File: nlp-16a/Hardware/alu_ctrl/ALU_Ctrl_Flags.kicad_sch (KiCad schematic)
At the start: 18 parts, among them U1 CD74HC00, U10 CD74HC00, U11 CD74HC00, U12 CD74HC00, U13 CD74HC00, U14 CD74HC00, U15 CD74HC00, U16 CD74HC00, U17 CD74HC00, U18 CD74HC00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

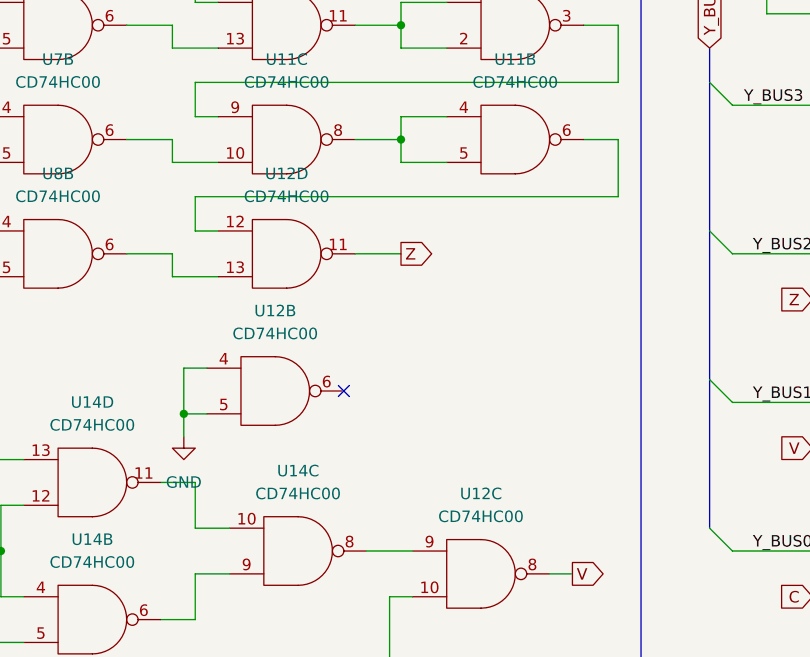
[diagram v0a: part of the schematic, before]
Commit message: ALU制御の回路修正
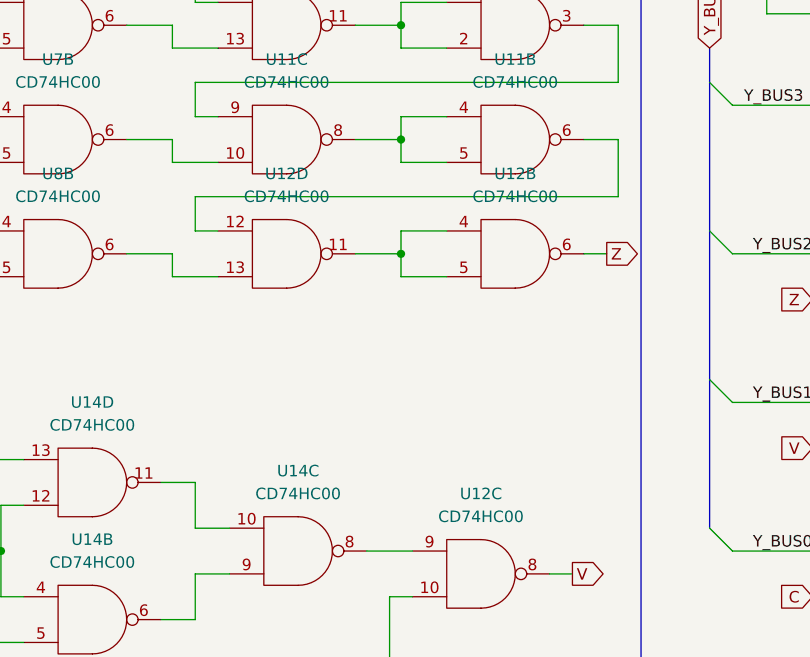
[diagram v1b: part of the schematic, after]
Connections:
- net GND: no longer U12.4, U12.5
- net Z: now also U12.6; no longer U12.11
- new net: U12.11, U12.4, U12.5
- no-connect marks 1 -> 0
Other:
- moved on the sheet: U12B
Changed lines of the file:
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@@
   (junction (at 64.77 22.86) (diameter 0) (color 0 0 0 0)
   )
+  (junction (at 163.83 116.84) (diameter 0) (color 0 0 0 0)
+  )
   (junction (at 163.83 91.44) (diameter 0) (color 0 0 0 0)
   )
@@
   (junction (at 36.83 53.34) (diameter 0) (color 0 0 0 0)
   )
-  (junction (at 139.7 134.62) (diameter 0) (color 0 0 0 0)
-  )
   (junction (at 212.09 90.17) (diameter 0) (color 0 0 0 0)
   )
@@
   (junction (at 163.83 66.04) (diameter 0) (color 0 0 0 0)
   )
-  (no_connect (at 157.48 132.08))
   (bus_entry (at 13.97 83.82) (size 2.54 2.54)
     (stroke (width 0) (type default) (color 0 0 0 0))
@@
     (stroke (width 0) (type default) (color 0 0 0 0))
   )
-  (wire (pts (xy 139.7 134.62) (xy 142.24 134.62))
+  (wire (pts (xy 163.83 119.38) (xy 168.91 119.38))
     (stroke (width 0) (type default) (color 0 0 0 0))
   )
@@
     (stroke (width 0) (type default) (color 0 0 0 0))
   )
-  (wire (pts (xy 142.24 129.54) (xy 139.7 129.54))
+  (wire (pts (xy 168.91 114.3) (xy 163.83 114.3))
     (stroke (width 0) (type default) (color 0 0 0 0))
   )
@@
     (stroke (width 0) (type default) (color 0 0 0 0))
   )
+  (wire (pts (xy 186.69 116.84) (xy 184.15 116.84))
+    (stroke (width 0) (type default) (color 0 0 0 0))
+  )
   (wire (pts (xy 35.56 137.16) (xy 38.1 137.16))
     (stroke (width 0) (type default) (color 0 0 0 0))
@@
     (stroke (width 0) (type default) (color 0 0 0 0))
   )
-  (wire (pts (xy 139.7 134.62) (xy 139.7 137.16))
-    (stroke (width 0) (type default) (color 0 0 0 0))
-  )
   (wire (pts (xy 64.77 68.58) (xy 64.77 63.5))
     (stroke (width 0) (type default) (color 0 0 0 0))
@@
     (stroke (width 0) (type default) (color 0 0 0 0))
   )
-  (wire (pts (xy 139.7 129.54) (xy 139.7 134.62))
+  (wire (pts (xy 163.83 114.3) (xy 163.83 116.84))
     (stroke (width 0) (type default) (color 0 0 0 0))
   )
@@
   )
   (wire (pts (xy 113.03 78.74) (xy 113.03 76.2))
+    (stroke (width 0) (type default) (color 0 0 0 0))
+  )
+  (wire (pts (xy 163.83 116.84) (xy 163.83 119.38))
     (stroke (width 0) (type default) (color 0 0 0 0))
   )
@@
     )
   )
-  (global_label "Z" (shape output) (at 163.83 116.84 0) (fields_autoplaced)
+  (global_label "Z" (shape output) (at 186.69 116.84 0) (fields_autoplaced)
     (effects (font (size 1.27 1.27)) (justify left))
-    (property "Intersheet References" "${INTERSHEET_REFS}" (id 0) (at 167.4526 116.7606 0)
+    (property "Intersheet References" "${INTERSHEET_REFS}" (id 0) (at 190.3126 116.7606 0)
       (effects (font (size 1.27 1.27)) (justify left) hide)
     )
@@
     (pin "13")
   )
-  (symbol (lib_id "CD74HCxx:CD74HC00") (at 149.86 132.08 0) (unit 2)
+  (symbol (lib_id "CD74HCxx:CD74HC00") (at 176.53 116.84 0) (unit 2)
     (in_bom yes) (on_board yes)
-    (property "Reference" "U12" (id 0) (at 149.86 123.19 0))
-    (property "Value" "CD74HC00" (id 1) (at 149.86 125.73 0))
-    (property "Footprint" "Package_DIP:DIP-14_W7.62mm" (id 2) (at 144.78 132.08 0)
-      (effects (font (size 1.27 1.27)) hide)
-    )
-    (property "Datasheet" "" (id 3) (at 144.78 132.08 0))
+    (property "Reference" "U12" (id 0) (at 176.53 107.95 0))
+    (property "Value" "CD74HC00" (id 1) (at 176.53 110.49 0))
+    (property "Footprint" "Package_DIP:DIP-14_W7.62mm" (id 2) (at 171.45 116.84 0)
+      (effects (font (size 1.27 1.27)) hide)
+    )
+    (property "Datasheet" "" (id 3) (at 171.45 116.84 0))
     (pin "14")
     (pin "7")
@@
     (pin "13")
   )
-  (symbol (lib_id "power:GND") (at 139.7 137.16 0) (unit 1)
-    (in_bom yes) (on_board yes) (fields_autoplaced)
-    (property "Reference" "#PWR0102" (id 0) (at 139.7 143.51 0)
-      (effects (font (size 1.27 1.27)) hide)
-    )
-    (property "Value" "GND" (id 1) (at 139.7 142.24 0))
-    (property "Footprint" "" (id 2) (at 139.7 137.16 0)
-      (effects (font (size 1.27 1.27)) hide)
-    )
-    (property "Datasheet" "" (id 3) (at 139.7 137.16 0)
-      (effects (font (size 1.27 1.27)) hide)
-    )
-    (pin "1")
-  )
   (symbol (lib_id "CD74HCxx:CD74HC00") (at 74.93 53.34 0) (unit 4)

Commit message: ゼロフラグ高速化
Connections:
- net Z: now also U9.3; no longer U12.6
- net at U9.13: now also U9.6; no longer U2.6
- net at U10.12: now also U3.6; no longer U9.6
- net at U10.13: now also U10.6; no longer U4.6
- net at U11.10: now also U12.6; no longer U7.6
- net at U11.9: now also U6.6; no longer U11.3
- net at U9.9: now also U2.6; no longer U9.3
- net at U12.12: now also U7.6; no longer U11.6
- net at U11.13: now also U11.6; no longer U6.6
- net at U11.12: now also U5.6; no longer U10.6
- net at U9.10: now also U10.3; no longer U3.6
- net at U10.10: now also U11.3; no longer U5.6
- net at U10.9: now also U4.6; no longer U10.3
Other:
- moved on the sheet: U10A, U10B, U10C, U10D, U11A, U11B, U11C, U11D, U12B, U12D, U9A, U9B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

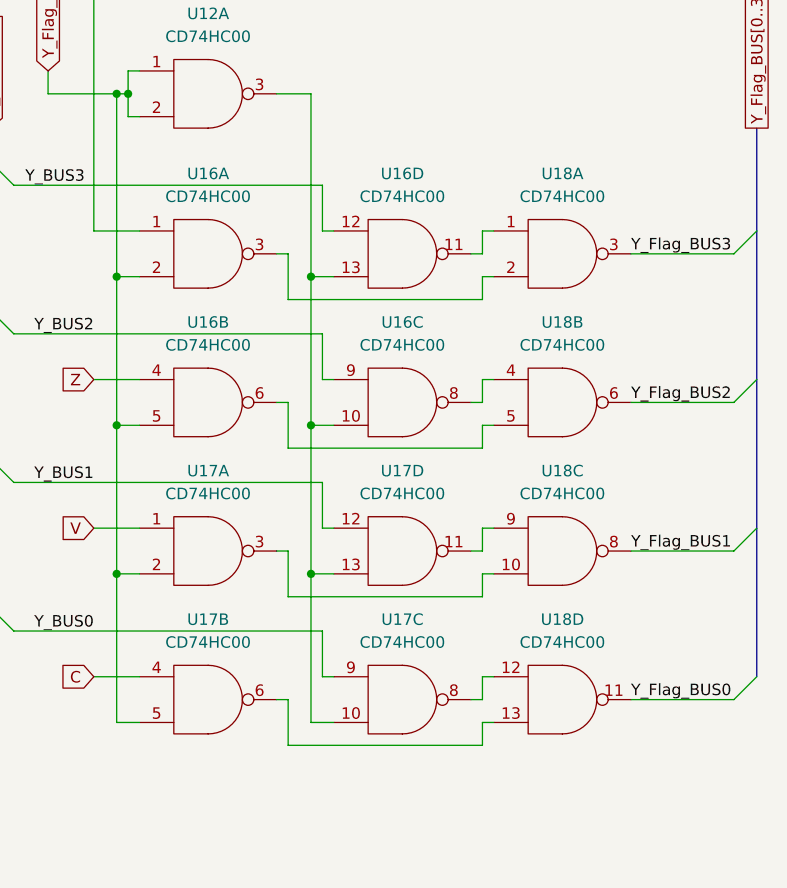
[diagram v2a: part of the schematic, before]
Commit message: 基板の途中経過(デコーダ部分を配線中)
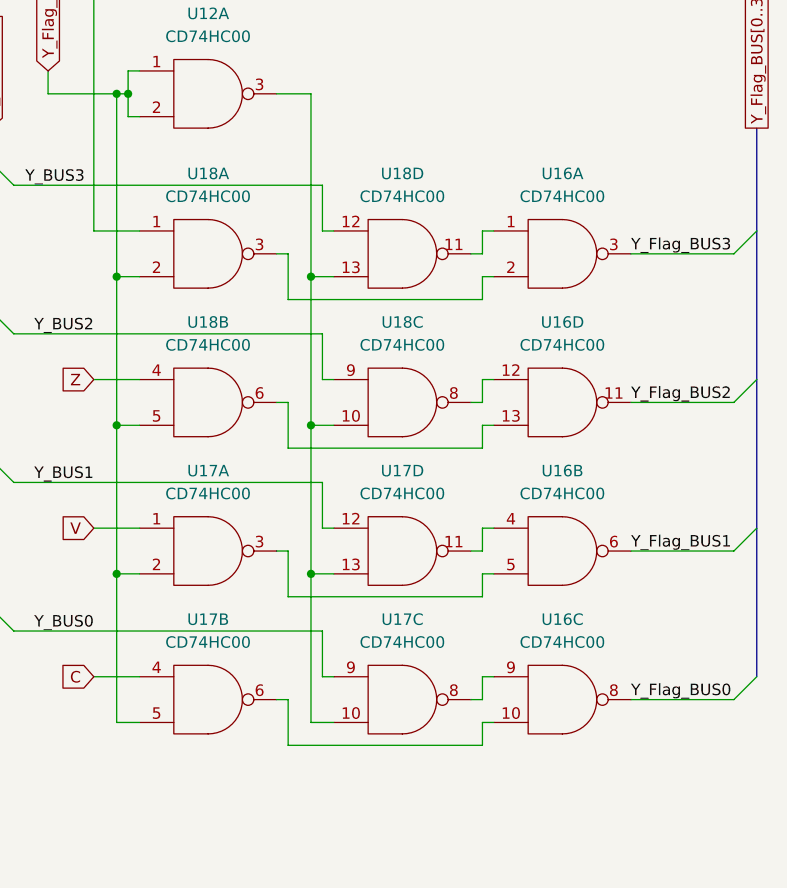
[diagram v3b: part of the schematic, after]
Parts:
- renumbered U18 to U16, U16 to U18
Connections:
- net Y_Flag_BUS0: now also U16.8; no longer U16.11
- net Y_Flag_BUS1: now also U16.6; no longer U16.8
- net Y_Flag_BUS2: now also U16.11; no longer U16.6
- net at U17.3: now also U16.5; no longer U16.10
- net at U18.8: now also U16.12; no longer U16.4
- net at U18.6: now also U16.13; no longer U16.5
- net at U17.6: now also U16.10; no longer U16.13
- net at U17.11: now also U16.4; no longer U16.9
- net at U17.8: now also U16.9; no longer U16.12
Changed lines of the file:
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@@
   (symbol (lib_id "CD74HCxx:CD74HC00") (at 222.25 107.95 0) (unit 1)
     (in_bom yes) (on_board yes) (fields_autoplaced)
-    (property "Reference" "U16" (id 0) (at 222.25 99.06 0))
+    (property "Reference" "U18" (id 0) (at 222.25 99.06 0))
     (property "Value" "CD74HC00" (id 1) (at 222.25 101.6 0))
     (property "Footprint" "Package_DIP:DIP-14_W7.62mm" (id 2) (at 217.17 107.95 0)
@@
   (symbol (lib_id "CD74HCxx:CD74HC00") (at 243.84 124.46 0) (unit 3)
     (in_bom yes) (on_board yes) (fields_autoplaced)
-    (property "Reference" "U16" (id 0) (at 243.84 115.57 0))
+    (property "Reference" "U18" (id 0) (at 243.84 115.57 0))
     (property "Value" "CD74HC00" (id 1) (at 243.84 118.11 0))
     (property "Footprint" "Package_DIP:DIP-14_W7.62mm" (id 2) (at 238.76 124.46 0)
@@
     (pin "13")
   )
-  (symbol (lib_id "CD74HCxx:CD74HC00") (at 261.62 124.46 0) (unit 2)
-    (in_bom yes) (on_board yes) (fields_autoplaced)
-    (property "Reference" "U18" (id 0) (at 261.62 115.57 0))
+  (symbol (lib_id "CD74HCxx:CD74HC00") (at 261.62 124.46 0) (unit 4)
+    (in_bom yes) (on_board yes) (fields_autoplaced)
+    (property "Reference" "U16" (id 0) (at 261.62 115.57 0))
     (property "Value" "CD74HC00" (id 1) (at 261.62 118.11 0))
     (property "Footprint" "Package_DIP:DIP-14_W7.62mm" (id 2) (at 256.54 124.46 0)
@@
   (symbol (lib_id "CD74HCxx:CD74HC00") (at 222.25 124.46 0) (unit 2)
     (in_bom yes) (on_board yes) (fields_autoplaced)
-    (property "Reference" "U16" (id 0) (at 222.25 115.57 0))
+    (property "Reference" "U18" (id 0) (at 222.25 115.57 0))
     (property "Value" "CD74HC00" (id 1) (at 222.25 118.11 0))
     (property "Footprint" "Package_DIP:DIP-14_W7.62mm" (id 2) (at 217.17 124.46 0)
@@
   (symbol (lib_id "CD74HCxx:CD74HC00") (at 243.84 107.95 0) (unit 4)
     (in_bom yes) (on_board yes) (fields_autoplaced)
-    (property "Reference" "U16" (id 0) (at 243.84 99.06 0))
+    (property "Reference" "U18" (id 0) (at 243.84 99.06 0))
     (property "Value" "CD74HC00" (id 1) (at 243.84 101.6 0))
     (property "Footprint" "Package_DIP:DIP-14_W7.62mm" (id 2) (at 238.76 107.95 0)
@@
     (pin "13")
   )
-  (symbol (lib_id "CD74HCxx:CD74HC00") (at 261.62 157.48 0) (unit 4)
-    (in_bom yes) (on_board yes) (fields_autoplaced)
-    (property "Reference" "U18" (id 0) (at 261.62 148.59 0))
+  (symbol (lib_id "CD74HCxx:CD74HC00") (at 261.62 157.48 0) (unit 3)
+    (in_bom yes) (on_board yes) (fields_autoplaced)
+    (property "Reference" "U16" (id 0) (at 261.62 148.59 0))
     (property "Value" "CD74HC00" (id 1) (at 261.62 151.13 0))
     (property "Footprint" "Package_DIP:DIP-14_W7.62mm" (id 2) (at 256.54 157.48 0)
@@
     (pin "13")
   )
-  (symbol (lib_id "CD74HCxx:CD74HC00") (at 261.62 140.97 0) (unit 3)
-    (in_bom yes) (on_board yes) (fields_autoplaced)
-    (property "Reference" "U18" (id 0) (at 261.62 132.08 0))
+  (symbol (lib_id "CD74HCxx:CD74HC00") (at 261.62 140.97 0) (unit 2)
+    (in_bom yes) (on_board yes) (fields_autoplaced)
+    (property "Reference" "U16" (id 0) (at 261.62 132.08 0))
     (property "Value" "CD74HC00" (id 1) (at 261.62 134.62 0))
     (property "Footprint" "Package_DIP:DIP-14_W7.62mm" (id 2) (at 256.54 140.97 0)
@@
   (symbol (lib_id "CD74HCxx:CD74HC00") (at 261.62 107.95 0) (unit 1)
     (in_bom yes) (on_board yes) (fields_autoplaced)
-    (property "Reference" "U18" (id 0) (at 261.62 99.06 0))
+    (property "Reference" "U16" (id 0) (at 261.62 99.06 0))
     (property "Value" "CD74HC00" (id 1) (at 261.62 101.6 0))
     (property "Footprint" "Package_DIP:DIP-14_W7.62mm" (id 2) (at 256.54 107.95 0)

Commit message: 基板の途中経過
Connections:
- net V: now also U12.6; no longer U12.8
- net Z: now also U12.8; no longer U9.3
- net at U9.12: now also U2.6; no longer U1.6
- net at U9.13: now also U1.6; no longer U9.6
- net at U10.12: now also U4.6; no longer U3.6
- net at U10.13: now also U9.6; no longer U10.6
- net at U11.10: now also U7.6; no longer U12.6
- net at U11.9: now also U11.3; no longer U6.6
- net at U15.8: now also U12.5; no longer U12.10
- net at U14.8: now also U12.4; no longer U12.9
- net at U12.12: now also U8.6; no longer U7.6
- net at U10.9: now also U10.3; no longer U4.6
- net at U10.10: now also U5.6; no longer U11.3
- net at U12.13: now also U11.6; no longer U8.6
- net at U11.12: now also U6.6; no longer U5.6
- net at U11.13: now also U10.6; no longer U11.6
- net at U9.10: now also U3.6; no longer U10.3
- net at U9.9: now also U9.3; no longer U2.6
- new net: U12.10, U12.11, U12.9
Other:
- note added: "配線の容易さを優先し，最速の接続ではない"
- moved on the sheet: U10A, U10B, U10C, U10D, U11A, U11B, U11C, U11D, U12C, U12D, U9A, U9B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

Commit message: デコーダ周りの配線が通った!
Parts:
- renumbered U18 to U16, U17 to U16, U18 to U17, U16 to U18
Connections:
- net C: now also U16.9; no longer U16.4
- net V: now also U16.4; no longer U16.1
- net Y_BUS1: now also U17.4; no longer U17.12
- net Y_BUS2: now also U17.12; no longer U17.9
- net Y_BUS3: now also U17.1; no longer U17.12
- net Y_Flag_sel: now also U16.10, U16.13, U16.5; no longer U16.2, U16.5, U16.5
- net Z: now also U16.12; no longer U16.4
- net at U18.5: now also U16.6; no longer U16.3
- net at U18.12: now also U16.11; no longer U17.8
- net at U18.13: now also U17.11; no longer U16.6
- net at U18.10: now also U17.8; no longer U16.6
- net at U18.4: now also U17.6; no longer U17.11
- net at U18.1: now also U17.3; no longer U17.11
- net at U18.9: now also U16.8; no longer U17.8
- new net: U12.3, U17.10, U17.13, U17.2, U17.5
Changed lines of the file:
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@@
   (symbol (lib_id "CD74HCxx:CD74HC00") (at 222.25 107.95 0) (unit 1)
     (in_bom yes) (on_board yes) (fields_autoplaced)
-    (property "Reference" "U18" (id 0) (at 222.25 99.06 0))
+    (property "Reference" "U16" (id 0) (at 222.25 99.06 0))
     (property "Value" "CD74HC00" (id 1) (at 222.25 101.6 0))
     (property "Footprint" "Package_DIP:DIP-14_W7.62mm" (id 2) (at 217.17 107.95 0)
@@
     (pin "13")
   )
-  (symbol (lib_id "CD74HCxx:CD74HC00") (at 222.25 140.97 0) (unit 1)
-    (in_bom yes) (on_board yes) (fields_autoplaced)
-    (property "Reference" "U17" (id 0) (at 222.25 132.08 0))
+  (symbol (lib_id "CD74HCxx:CD74HC00") (at 222.25 140.97 0) (unit 2)
+    (in_bom yes) (on_board yes) (fields_autoplaced)
+    (property "Reference" "U16" (id 0) (at 222.25 132.08 0))
     (property "Value" "CD74HC00" (id 1) (at 222.25 134.62 0))
     (property "Footprint" "Package_DIP:DIP-14_W7.62mm" (id 2) (at 217.17 140.97 0)
@@
     (pin "13")
   )
-  (symbol (lib_id "CD74HCxx:CD74HC00") (at 243.84 124.46 0) (unit 3)
-    (in_bom yes) (on_board yes) (fields_autoplaced)
-    (property "Reference" "U18" (id 0) (at 243.84 115.57 0))
+  (symbol (lib_id "CD74HCxx:CD74HC00") (at 243.84 124.46 0) (unit 4)
+    (in_bom yes) (on_board yes) (fields_autoplaced)
+    (property "Reference" "U17" (id 0) (at 243.84 115.57 0))
     (property "Value" "CD74HC00" (id 1) (at 243.84 118.11 0))
     (property "Footprint" "Package_DIP:DIP-14_W7.62mm" (id 2) (at 238.76 124.46 0)
@@
     (pin "13")
   )
-  (symbol (lib_id "CD74HCxx:CD74HC00") (at 261.62 124.46 0) (unit 4)
-    (in_bom yes) (on_board yes) (fields_autoplaced)
-    (property "Reference" "U16" (id 0) (at 261.62 115.57 0))
+  (symbol (lib_id "CD74HCxx:CD74HC00") (at 261.62 124.46 0) (mirror x) (unit 4)
+    (in_bom yes) (on_board yes) (fields_autoplaced)
+    (property "Reference" "U18" (id 0) (at 261.62 115.57 0))
     (property "Value" "CD74HC00" (id 1) (at 261.62 118.11 0))
     (property "Footprint" "Package_DIP:DIP-14_W7.62mm" (id 2) (at 256.54 124.46 0)
@@
     (pin "13")
   )
-  (symbol (lib_id "CD74HCxx:CD74HC00") (at 222.25 157.48 0) (unit 2)
-    (in_bom yes) (on_board yes) (fields_autoplaced)
-    (property "Reference" "U17" (id 0) (at 222.25 148.59 0))
+  (symbol (lib_id "CD74HCxx:CD74HC00") (at 222.25 157.48 0) (unit 3)
+    (in_bom yes) (on_board yes) (fields_autoplaced)
+    (property "Reference" "U16" (id 0) (at 222.25 148.59 0))
     (property "Value" "CD74HC00" (id 1) (at 222.25 151.13 0))
     (property "Footprint" "Package_DIP:DIP-14_W7.62mm" (id 2) (at 217.17 157.48 0)
@@
     (pin "13")
   )
-  (symbol (lib_id "CD74HCxx:CD74HC00") (at 243.84 140.97 0) (unit 4)
+  (symbol (lib_id "CD74HCxx:CD74HC00") (at 243.84 140.97 0) (unit 2)
     (in_bom yes) (on_board yes) (fields_autoplaced)
     (property "Reference" "U17" (id 0) (at 243.84 132.08 0))
@@
     (pin "13")
   )
-  (symbol (lib_id "CD74HCxx:CD74HC00") (at 222.25 124.46 0) (unit 2)
-    (in_bom yes) (on_board yes) (fields_autoplaced)
-    (property "Reference" "U18" (id 0) (at 222.25 115.57 0))
+  (symbol (lib_id "CD74HCxx:CD74HC00") (at 222.25 124.46 0) (unit 4)
+    (in_bom yes) (on_board yes) (fields_autoplaced)
+    (property "Reference" "U16" (id 0) (at 222.25 115.57 0))
     (property "Value" "CD74HC00" (id 1) (at 222.25 118.11 0))
     (property "Footprint" "Package_DIP:DIP-14_W7.62mm" (id 2) (at 217.17 124.46 0)
@@
     (pin "13")
   )
-  (symbol (lib_id "CD74HCxx:CD74HC00") (at 243.84 107.95 0) (unit 4)
-    (in_bom yes) (on_board yes) (fields_autoplaced)
-    (property "Reference" "U18" (id 0) (at 243.84 99.06 0))
+  (symbol (lib_id "CD74HCxx:CD74HC00") (at 243.84 107.95 0) (unit 1)
+    (in_bom yes) (on_board yes) (fields_autoplaced)
+    (property "Reference" "U17" (id 0) (at 243.84 99.06 0))
     (property "Value" "CD74HC00" (id 1) (at 243.84 101.6 0))
     (property "Footprint" "Package_DIP:DIP-14_W7.62mm" (id 2) (at 238.76 107.95 0)
@@
     (pin "13")
   )
-  (symbol (lib_id "CD74HCxx:CD74HC00") (at 261.62 157.48 0) (unit 3)
-    (in_bom yes) (on_board yes) (fields_autoplaced)
-    (property "Reference" "U16" (id 0) (at 261.62 148.59 0))
+  (symbol (lib_id "CD74HCxx:CD74HC00") (at 261.62 157.48 0) (mirror x) (unit 3)
+    (in_bom yes) (on_board yes) (fields_autoplaced)
+    (property "Reference" "U18" (id 0) (at 261.62 148.59 0))
     (property "Value" "CD74HC00" (id 1) (at 261.62 151.13 0))
     (property "Footprint" "Package_DIP:DIP-14_W7.62mm" (id 2) (at 256.54 157.48 0)
@@
   (symbol (lib_id "CD74HCxx:CD74HC00") (at 261.62 140.97 0) (unit 2)
     (in_bom yes) (on_board yes) (fields_autoplaced)
-    (property "Reference" "U16" (id 0) (at 261.62 132.08 0))
+    (property "Reference" "U18" (id 0) (at 261.62 132.08 0))
     (property "Value" "CD74HC00" (id 1) (at 261.62 134.62 0))
     (property "Footprint" "Package_DIP:DIP-14_W7.62mm" (id 2) (at 256.54 140.97 0)
@@
   (symbol (lib_id "CD74HCxx:CD74HC00") (at 261.62 107.95 0) (unit 1)
     (in_bom yes) (on_board yes) (fields_autoplaced)
-    (property "Reference" "U16" (id 0) (at 261.62 99.06 0))
+    (property "Reference" "U18" (id 0) (at 261.62 99.06 0))
     (property "Value" "CD74HC00" (id 1) (at 261.62 101.6 0))
     (property "Footprint" "Package_DIP:DIP-14_W7.62mm" (id 2) (at 256.54 107.95 0)
